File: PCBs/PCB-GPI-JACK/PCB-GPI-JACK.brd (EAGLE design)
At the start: 57 x 44 mm, 51 parts, among them IC2 MCP23017SS, X1 DB25F

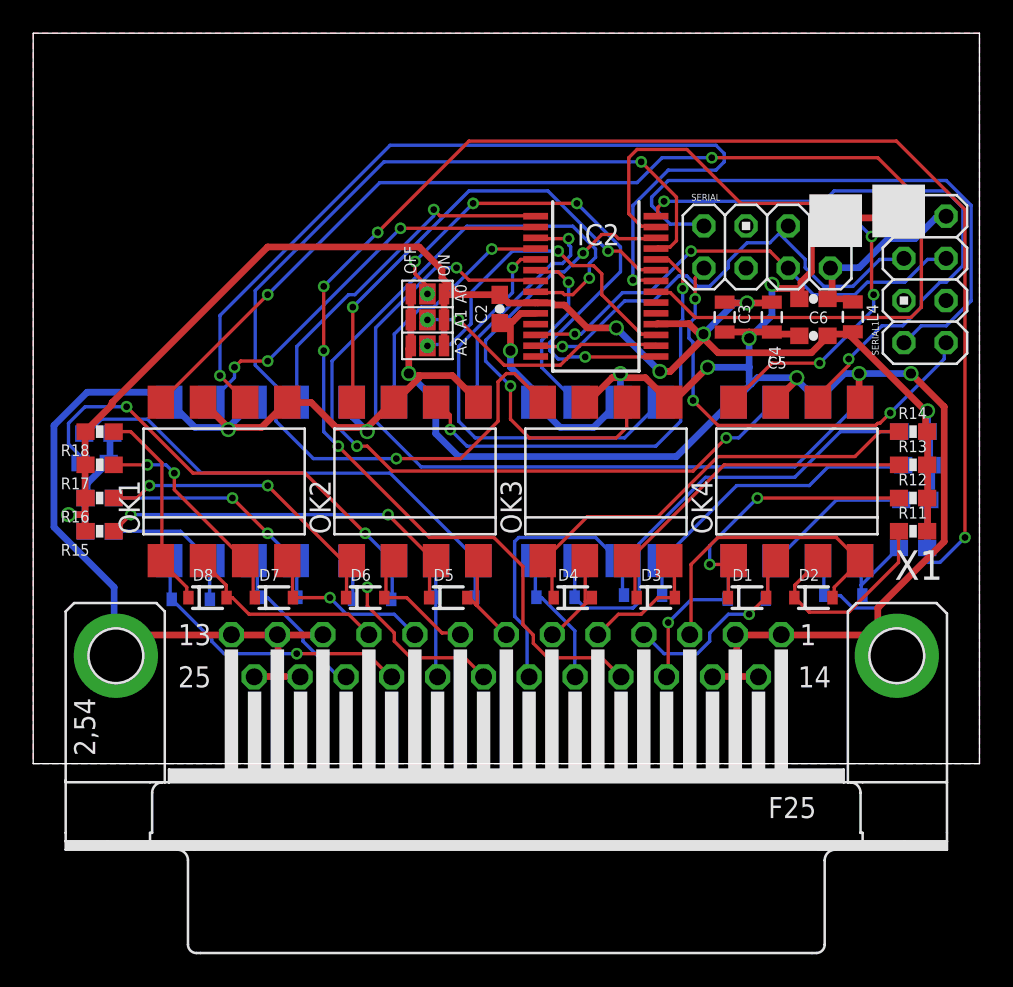
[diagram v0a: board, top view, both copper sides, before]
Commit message: size of board
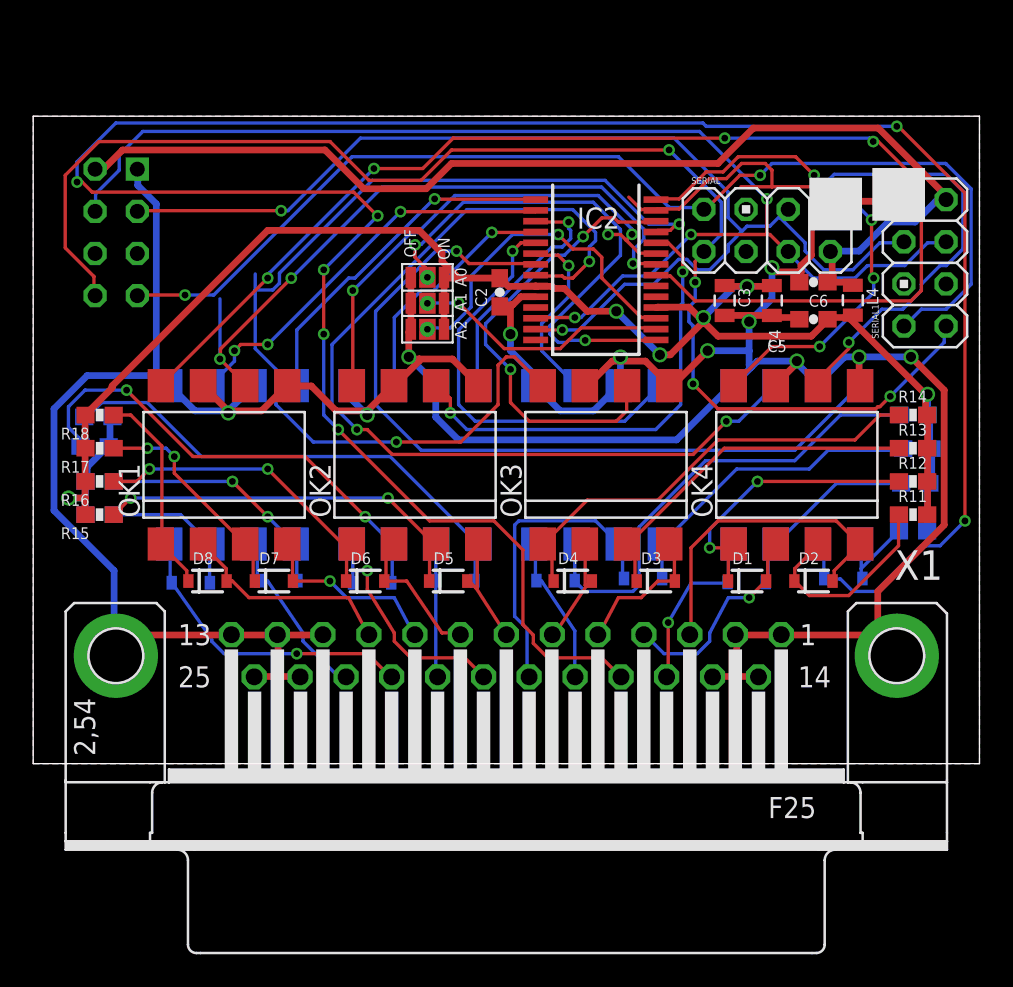
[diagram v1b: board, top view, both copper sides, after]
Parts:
- added SERIAL2: M04X2M2X4SMALLER, SKAARHOJ:M2X4SMALLER
- moved C2 1.00 mm to (28.1, 28.4)
- moved C3 1.00 mm to (41.6, 27.9)
- moved C4 1.00 mm to (44.5, 27.9)
- moved C5 1.00 mm to (47.0, 26.8)
- moved C6 1.00 mm to (47.0, 29.0)
- moved D1 1.00 mm to (43.0, 11.0)
- moved D10 1.00 mm to (48.8, 11.2)
- moved D11 1.00 mm to (31.5, 11.0)
- moved D12 1.00 mm to (36.7, 11.2)
- moved D13 1.00 mm to (20.4, 10.9)
- moved D14 1.00 mm to (25.4, 11.0)
- moved D15 1.00 mm to (9.49, 10.9)
- moved D16 1.00 mm to (14.8, 11.0)
- moved D2 1.00 mm to (47.0, 11.0)
- moved D3 1.00 mm to (37.5, 11.0)
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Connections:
- removed net N$2: C6.1, L4.1, SERIAL.2, SERIAL1.2
- new net N$3: C6.1, L4.1, SERIAL.2, SERIAL1.2, SERIAL2.2
- net GND: now also SERIAL2.1
- net I2C_SCL: now also SERIAL2.4
- net I2C_SDA: now also SERIAL2.3
- net SDI_MOSI: now also SERIAL2.8
- net SDI_SCLK: now also SERIAL2.7
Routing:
- net N$3: track 0.00 -> 68.1 mm
- net SDI_MOSI: track 26.9 -> 81.7 mm, vias 3 -> 4
- net I2C_SCL: track 28.8 -> 76.2 mm, vias 2 -> 3
- net I2C_SDA: track 29.4 -> 70.9 mm, vias 1 -> 2
- net N$10: track 111.6 -> 149.7 mm, vias 5 -> 7
- net SDI_SCLK: track 35.3 -> 67.8 mm, vias 0 -> 2
- net GND: track 205.0 -> 220.8 mm
- net IN2: track 53.7 -> 40.8 mm, vias 2 -> 3
- net N$2: track 11.9 -> 0.00 mm
- net IN7: track 37.6 -> 35.2 mm
- net IN5: track 63.2 -> 61.0 mm
- net IN8: track 36.1 -> 37.3 mm
- net IN3: track 28.9 -> 29.9 mm, vias 2 -> 3
- net N$7: track 7.11 -> 8.11 mm
- net N$66: track 18.7 -> 19.7 mm
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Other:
- board size 57 x 44 mm -> 57 x 39 mm
- board text added: "inverse"
